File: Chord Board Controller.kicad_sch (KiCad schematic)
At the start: 80 parts, among them J1 5 Pin Header 2.54mm, J4 HRO_TYPE-C-31-M-14, J8 Batt_1S, Q13 2N7002, SW6 SW_SPST, SW7 RST, SW8 SW_SPDT, U3 TPS63805YFFR, U4 TPS63805YFFR, U5 SRV05-4, U7 nRF52840_holyiot_18010, U8 BQ24075RGT

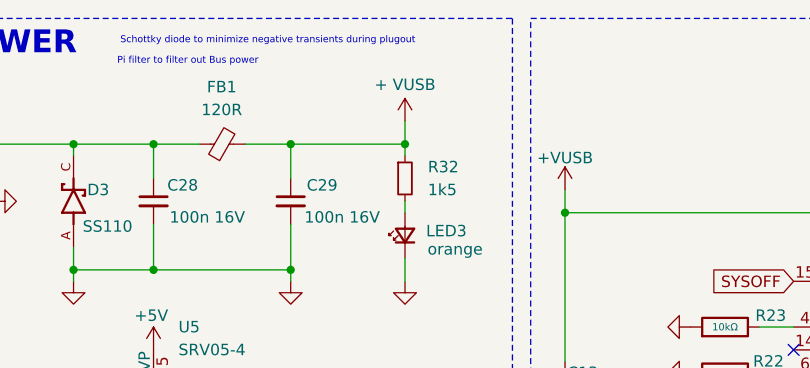
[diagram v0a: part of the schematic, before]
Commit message: gnd cutiings rmvd
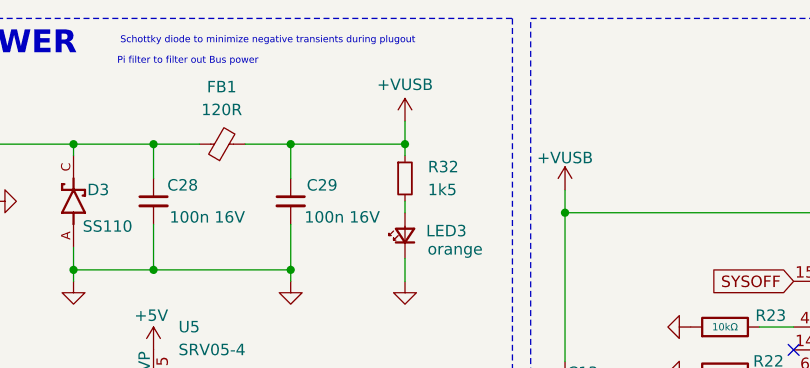
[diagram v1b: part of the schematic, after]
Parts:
- PG_LED1: footprint LED_THT:LED_D1.8mm_W1.8mm_H2.4mm_Horizontal_O6.35mm_Z8.2mm -> moshte:LED_0603
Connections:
- net + VUSB is gone; now on net +VUSB: C29.1, FB1.2, R32.1
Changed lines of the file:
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@@
 			)
 		)
-		(property "Value" "+ VUSB"
+		(property "Value" "+VUSB"
 			(at 132.08 21.336 0)
 			(effects
@@
 			)
 		)
-		(property "Footprint" "LED_THT:LED_D1.8mm_W1.8mm_H2.4mm_Horizontal_O6.35mm_Z8.2mm"
+		(property "Footprint" "moshte:LED_0603"
 			(at 219.71 46.99 90)
 			(effects

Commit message: post review
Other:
- note added: "Chord Board Controller"
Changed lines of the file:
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@@
+		)
+	)
+	(text "Chord Board Controller"
+		(exclude_from_sim no)
+		(at 351.536 276.606 0)
+		(effects
+			(font
+				(size 1.778 1.778)
+				(color 255 153 0 1)
+			)
 		)
 	)
